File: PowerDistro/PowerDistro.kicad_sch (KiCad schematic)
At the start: 13 parts

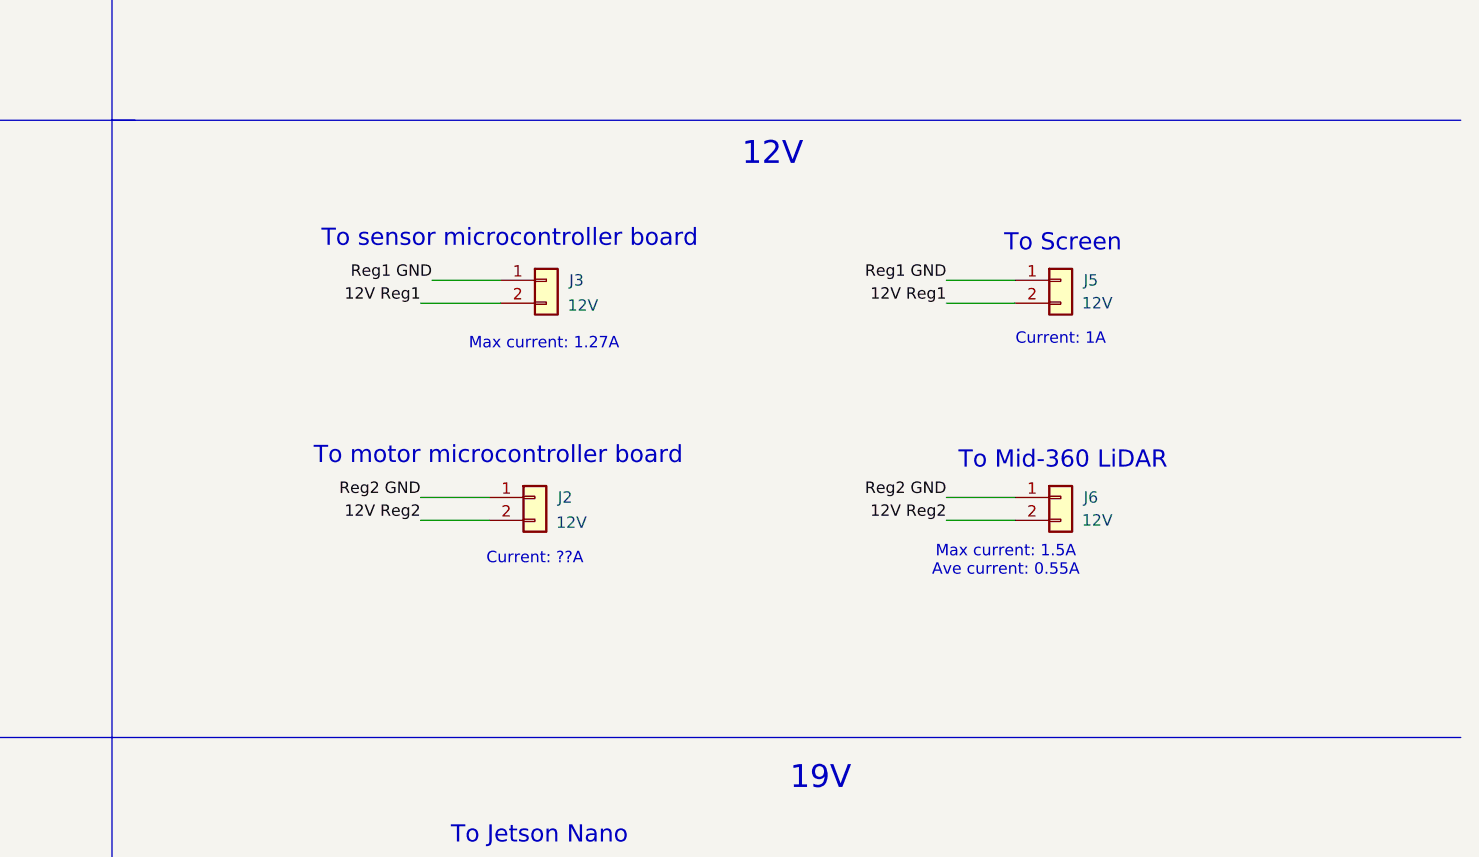
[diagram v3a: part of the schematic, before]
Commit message: Added transistor to turn on LiDAR
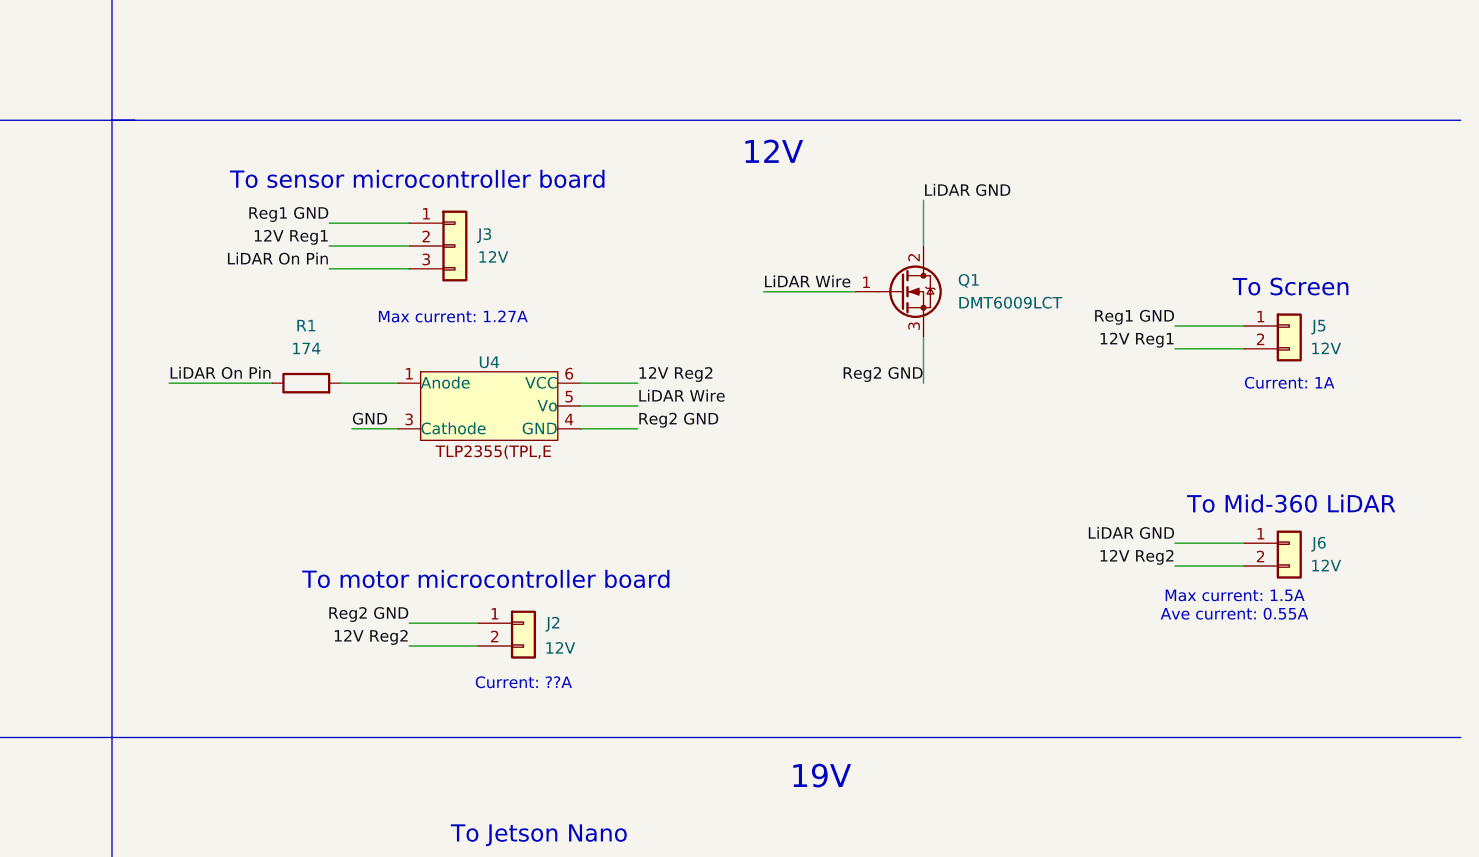
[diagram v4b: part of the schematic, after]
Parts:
- removed J3: ~, Connector_JST:JST_PH_S2B-PH-SM4-TB_1x02-1MP_P2.00mm_Horizontal, symbol Connector_Generic:Conn_01x02
- added J3: 12V, Connector_JST:JST_PH_S3B-PH-SM4-TB_1x03-1MP_P2.00mm_Horizontal, symbol Connector_Generic:Conn_01x03
- added Q1: DMT6009LCT, Package_TO_SOT_THT:TO-220-3_Vertical, symbol Device:Q_NMOS_GDS
- added R1: 174, Resistor_SMD:R_0805_2012Metric, symbol Device:R
- added U4: Optoisolators, Package_SO:SO-5-6_4.55x3.7mm_P1.27mm, symbol OptoIsolators:TLP2355(TPL,E
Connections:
- net 12V Reg1: now also J3.2 (Pin_2)
- net 12V Reg2: now also U4.6 (VCC)
- net Reg1 GND: now also J3.1 (Pin_1)
- net Reg2 GND: now also Q1.3 (S), U4.4 (GND); no longer J6.1 (Pin_1)
- new net: R1.2, U4.1 (Anode)
- new net GND: U4.3 (Cathode)
- new net LiDAR GND: J6.1 (Pin_1), Q1.2 (D)
- new net LiDAR On Pin: J3.3 (Pin_3), R1.1
- new net LiDAR Wire: Q1.1 (G), U4.5 (Vo)
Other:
- moved on the sheet: J2, J5, J6

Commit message: Updated PCB Layout
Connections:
- net GND is gone; now on net Reg1 GND: U4.3 (Cathode)

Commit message: Added part number for header
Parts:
- J3: Manufacturer Part Number (none) -> S3B-PH-SM4-TB

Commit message: Swapped to XH-A-1 connector and added mounting hole stencil cutouts
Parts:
- J4, J5, J6: footprint Connector_JST:JST_XH_S2B-XH-A_1x02_P2.50mm_Horizontal -> Connector_JST:JST_XH_S2B-XH-A-1_1x02_P2.50mm_Horizontal
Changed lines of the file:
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@@
 	(title_block
 		(title "Power Distribution Board")
-		(date "2025-02-06")
-		(rev "v1.0")
+		(date "2025-03-06")
+		(rev "v1.1")
 		(company "Lafyaette College")
 		(comment 1 "By Robbie Leslie")
